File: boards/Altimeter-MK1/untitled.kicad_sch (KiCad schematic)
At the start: 1 part

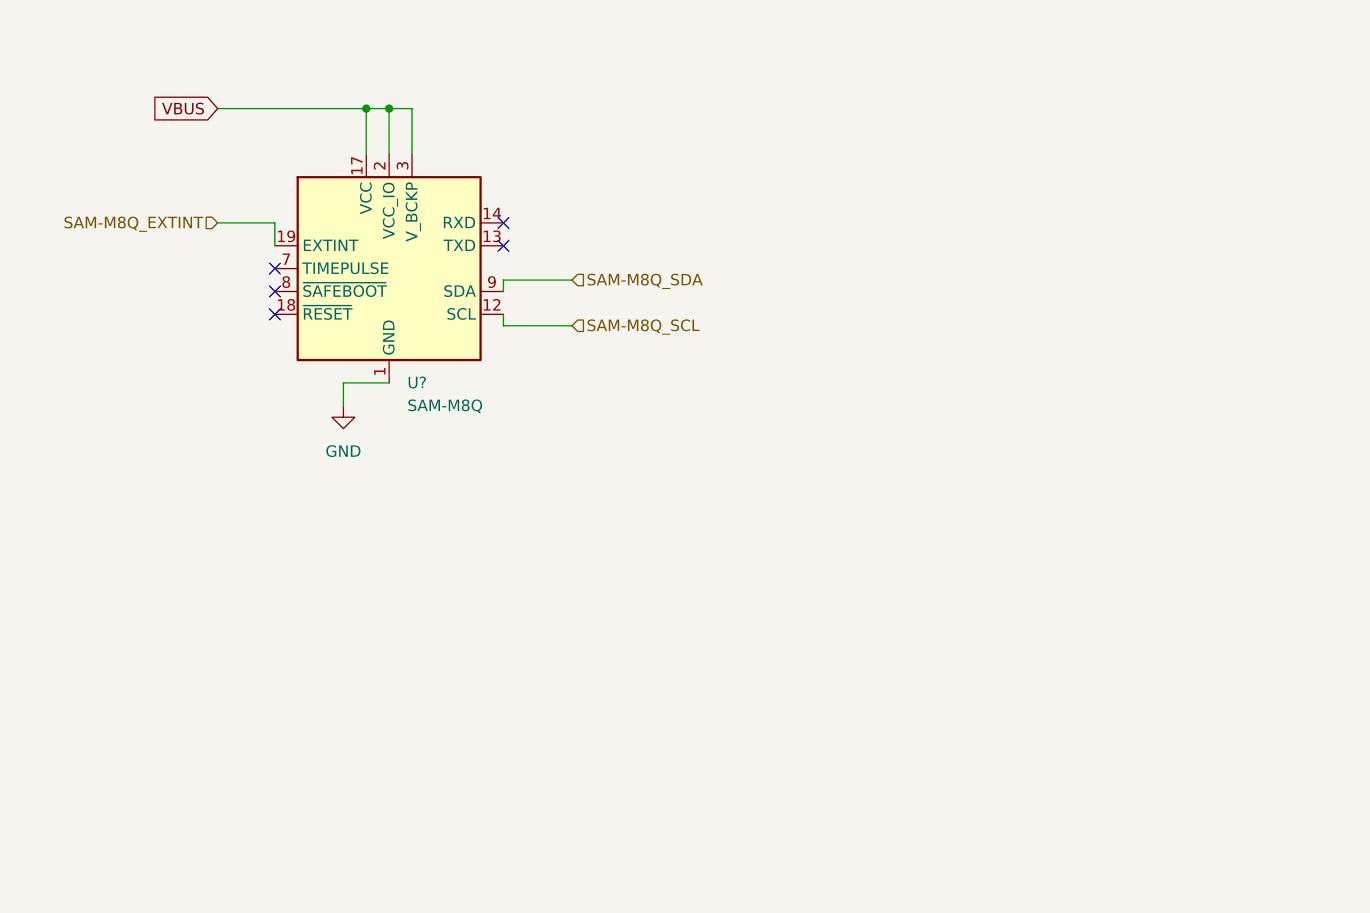
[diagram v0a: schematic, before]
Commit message: Left some comments and slightly cleaned up the schematic
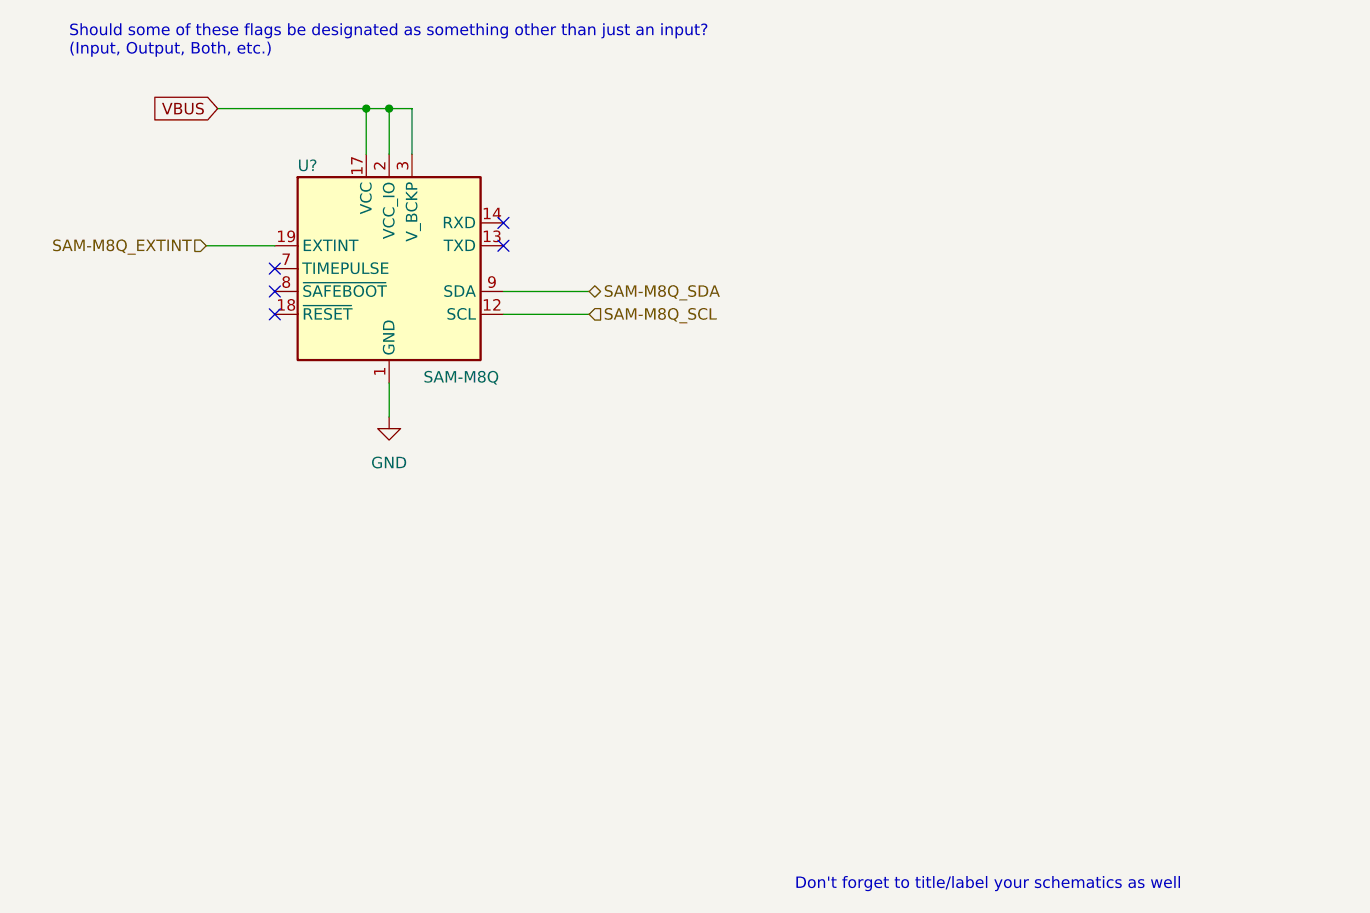
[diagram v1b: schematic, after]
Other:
- note added: "Don't forget to title/label your schematics as well"
- note added: "Should some of these flags be designated as something other than just an input? (Input, Output, Both, etc.)"
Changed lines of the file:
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@@
   (no_connect (at 130.81 95.25))
   (no_connect (at 130.81 92.71))
-  (wire (pts (xy 138.43 105.41) (xy 138.43 107.95))
-    (stroke (width 0) (type default) (color 0 0 0 0))
-  )
-  (wire (pts (xy 156.21 99.06) (xy 163.83 99.06))
+  (wire (pts (xy 156.21 97.79) (xy 165.735 97.79))
     (stroke (width 0) (type default) (color 0 0 0 0))
   )
@@
     (stroke (width 0) (type default) (color 0 0 0 0))
   )
-  (wire (pts (xy 143.51 105.41) (xy 138.43 105.41))
+  (wire (pts (xy 123.19 90.17) (xy 130.81 90.17))
     (stroke (width 0) (type default) (color 0 0 0 0))
   )
-  (wire (pts (xy 156.21 97.79) (xy 156.21 99.06))
-    (stroke (width 0) (type default) (color 0 0 0 0))
-  )
-  (wire (pts (xy 130.81 87.63) (xy 124.46 87.63))
-    (stroke (width 0) (type default) (color 0 0 0 0))
-  )
-  (wire (pts (xy 130.81 90.17) (xy 130.81 87.63))
-    (stroke (width 0) (type default) (color 0 0 0 0))
-  )
-  (wire (pts (xy 156.21 93.98) (xy 163.83 93.98))
+  (wire (pts (xy 156.21 95.25) (xy 165.735 95.25))
     (stroke (width 0) (type default) (color 0 0 0 0))
   )
   (wire (pts (xy 143.51 80.01) (xy 143.51 74.93))
+    (stroke (width 0) (type default) (color 0 0 0 0))
+  )
+  (wire (pts (xy 143.51 105.41) (xy 143.51 109.22))
     (stroke (width 0) (type default) (color 0 0 0 0))
   )
@@
     (stroke (width 0) (type default) (color 0 0 0 0))
   )
-  (wire (pts (xy 156.21 95.25) (xy 156.21 93.98))
-    (stroke (width 0) (type default) (color 0 0 0 0))
+  (text "Don't forget to title/label your schematics as well"
+    (at 188.595 161.925 0)
+    (effects (font (size 1.27 1.27)) (justify left bottom))
+  )
+  (text "Should some of these flags be designated as something other than just an input?\n(Input, Output, Both, etc.)"
+    (at 107.95 69.215 0)
+    (effects (font (size 1.27 1.27)) (justify left bottom))
   )
   (global_label "VBUS" (shape input) (at 124.46 74.93 180) (fields_autoplaced)
@@
     )
   )
-  (hierarchical_label "SAM-M8Q_EXTINT" (shape input) (at 124.46 87.63 180)
+  (hierarchical_label "SAM-M8Q_EXTINT" (shape input) (at 123.19 90.17 180)
     (effects (font (size 1.27 1.27)) (justify right))
   )
-  (hierarchical_label "SAM-M8Q_SCL" (shape input) (at 163.83 99.06 0)
+  (hierarchical_label "SAM-M8Q_SCL" (shape input) (at 165.735 97.79 0)
     (effects (font (size 1.27 1.27)) (justify left))
   )
-  (hierarchical_label "SAM-M8Q_SDA" (shape input) (at 163.83 93.98 0)
+  (hierarchical_label "SAM-M8Q_SDA" (shape bidirectional) (at 165.735 95.25 0)
     (effects (font (size 1.27 1.27)) (justify left))
   )
   (symbol (lib_id "RF_GPS:SAM-M8Q") (at 143.51 92.71 0) (unit 1)
-    (in_bom yes) (on_board yes) (fields_autoplaced)
-    (property "Reference" "U?" (id 0) (at 145.5294 105.41 0)
+    (in_bom yes) (on_board yes)
+    (property "Reference" "U?" (id 0) (at 133.35 81.28 0)
       (effects (font (size 1.27 1.27)) (justify left))
     )
-    (property "Value" "SAM-M8Q" (id 1) (at 145.5294 107.95 0)
+    (property "Value" "SAM-M8Q" (id 1) (at 147.32 104.775 0)
       (effects (font (size 1.27 1.27)) (justify left))
     )
@@
     (pin "9")
   )
-  (symbol (lib_id "power:GND") (at 138.43 107.95 0) (unit 1)
+  (symbol (lib_id "power:GND") (at 143.51 109.22 0) (unit 1)
     (in_bom yes) (on_board yes) (fields_autoplaced)
-    (property "Reference" "#PWR?" (id 0) (at 138.43 114.3 0)
+    (property "Reference" "#PWR?" (id 0) (at 143.51 115.57 0)
       (effects (font (size 1.27 1.27)) hide)
     )
-    (property "Value" "GND" (id 1) (at 138.43 113.03 0))
-    (property "Footprint" "" (id 2) (at 138.43 107.95 0)
+    (property "Value" "GND" (id 1) (at 143.51 114.3 0))
+    (property "Footprint" "" (id 2) (at 143.51 109.22 0)
       (effects (font (size 1.27 1.27)) hide)
     )
-    (property "Datasheet" "" (id 3) (at 138.43 107.95 0)
+    (property "Datasheet" "" (id 3) (at 143.51 109.22 0)
       (effects (font (size 1.27 1.27)) hide)
     )
